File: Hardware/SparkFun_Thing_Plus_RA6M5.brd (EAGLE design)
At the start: 22.9 x 71.1 mm, 93 parts, among them J1 USB Female Type C Connector, J2 THING_PLUS_LOGICAL, J3 QWIIC_RA, J4 CONN_03X2, J7 MICRO-SDFRICTION, Q2 20V/4.2A/52mΩ/1.4W, U1 R7FA6M5, U2 DA14531MOD, U3 MCP73831, U4 RT9080-33GJ5, U5 W25QXX128MBIT-6X5, U6 MCP1501-3.3V, U7 MAX17048, U8 LM66200, Y1 24.000MHz, Y2 32.768kHz

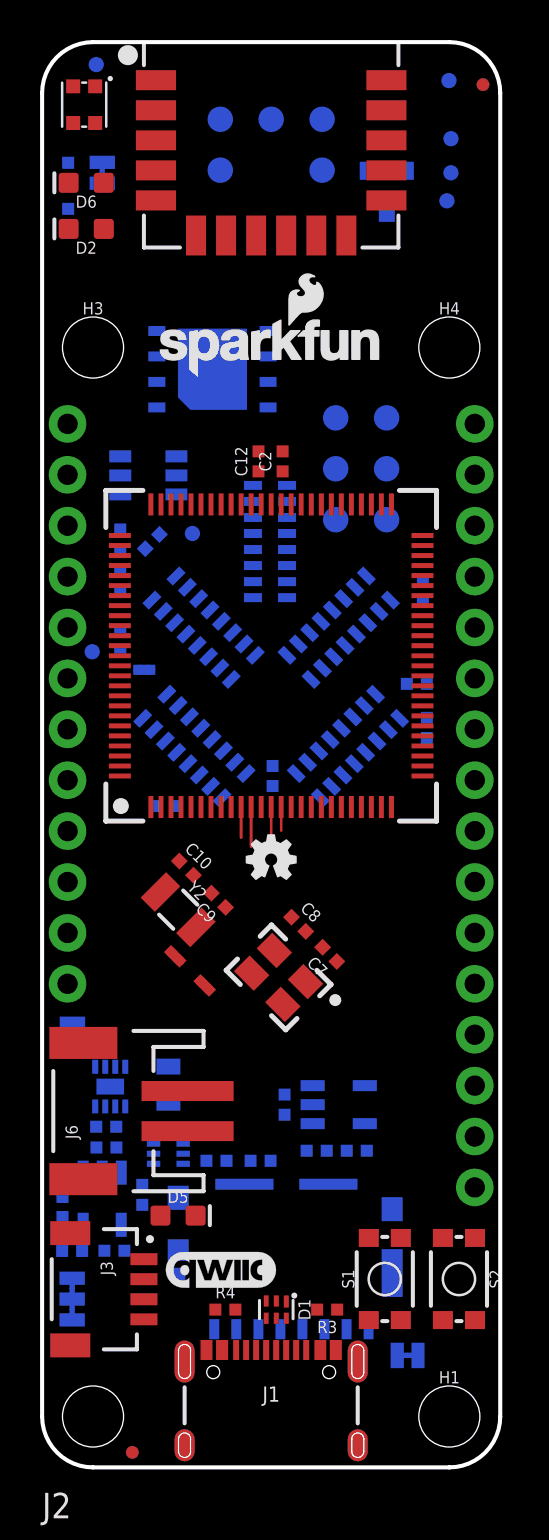
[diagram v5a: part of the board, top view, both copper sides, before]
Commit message: update based on pre-design review comments.
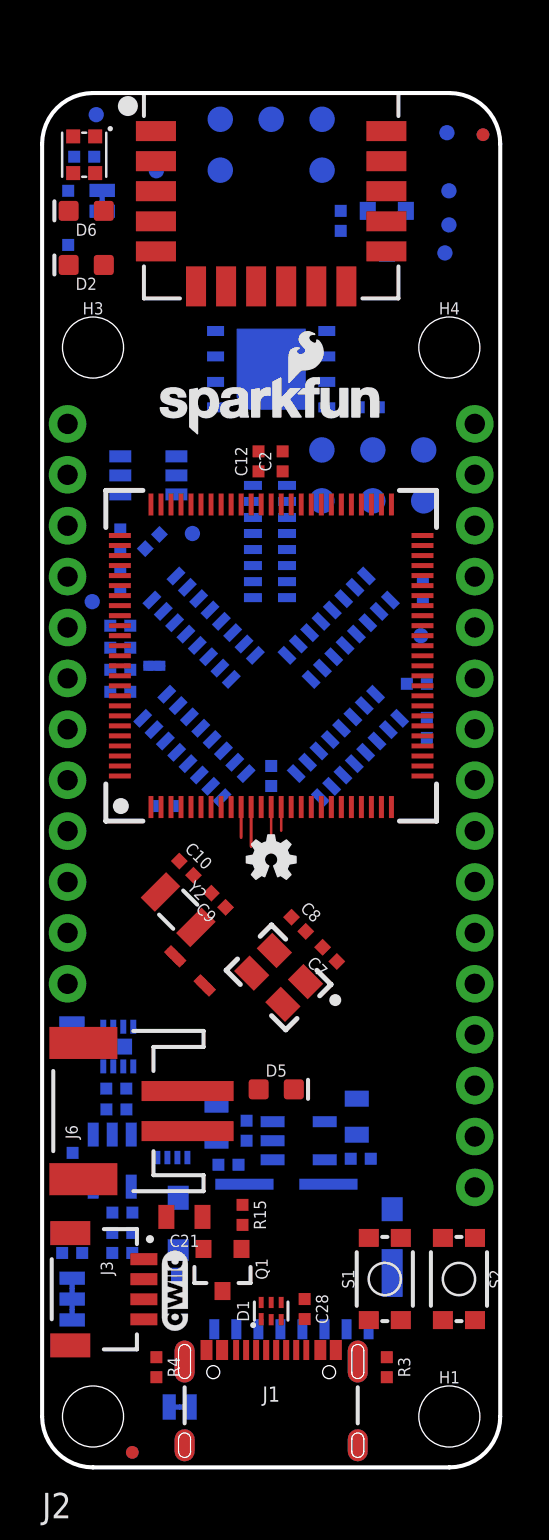
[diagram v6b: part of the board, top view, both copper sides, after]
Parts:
- removed JP1, JP3: JUMPER-SMT_2_NC_TRACE_SILK, SparkFun-Jumpers:SMT-JUMPER_2_NC_TRACE_SILK
- added C21: 10uF, SparkFun-Capacitors:0805
- added C22, C23, C25, C26, C28: 0.1uF, SparkFun-Capacitors:0402-TIGHT
- added C24: 47uF/6.3V, SparkFun-Capacitors:0805
- added C27: 1.0uF, SparkFun-Capacitors:0402-TIGHT
- added CHG, SHLD: JUMPER-SMT_2_NC_TRACE_SILK, SparkFun-Jumpers:SMT-JUMPER_2_NC_TRACE_SILK
- added Q1: 20V/4.2A/52mΩ/1.4W, SparkFun-DiscreteSemi:SOT23-3
- added R13, R15: 1k, SparkFun-Resistors:0402-TIGHT
- added TP9: TEST-POINT3, SparkFun-Connectors:PAD.03X.03
- added U$8: (no value), SparkFun-Aesthetics:SFE_LOGO_FLAME_STOP_.1
- LOGO3: value QWIIC_LOGO_CONNECTOR -> QWIIC_LOGO_4MM; device SparkFun-Aesthetics:QWIIC_5.5MM -> SparkFun-Aesthetics:QWIIC_4MM
- R10: value 10k -> 100k
- moved C1 10.1 mm to (1.50, 11.7), turned to 180 degrees
- moved D5 7.98 mm to (11.7, 18.9)
- moved R1 6.58 mm to (4.00, 10.7), turned to 180 degrees
- moved R4 4.49 mm to (5.70, 5.00), turned to 270 degrees
- moved C14 4.46 mm to (9.30, 15.1), turned to 0 degrees
- moved R3 4.14 mm to (17.2, 5.00), turned to 270 degrees
- moved C20 3.06 mm to (8.70, 17.2)
- moved U5 2.93 mm to (11.4, 54.8)
- moved LOGO2 2.88 mm to (11.4, 53.0)
- moved U4 2.69 mm to (12.8, 16.3)
- moved TP8 2.60 mm to (20.2, 66.6)
- moved TP3 2.60 mm to (20.1, 60.6)
- moved TP5 2.60 mm to (20.3, 63.7)
- moved TP7 2.60 mm to (20.3, 62.0)
- moved U2 2.54 mm to (11.4, 65.7)
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- renumbered JP2 to I2C
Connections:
- removed net N$25: RN3.15, U1.17
- removed net N$29: RN4.16, U1.40
- removed net N$34: RN4.9, U1.58
- removed net N$8: J5.6, Q2.1
- new net !DA14531_RST!: J5.6, R13.1, RN4.9, U1.58
- new net !NMI!: RN4.16, TP9.1, U1.40
- new net !SD_EN!: R15.1, RN3.1, U1.16
- new net 3.3V_SW: C28.2, J7.4, Q1.3
- new net N$4: Q2.1, R13.2
- new net N$47: Q1.1, R15.2
- net 3.3V: now also C21.1, C22.2, C23.2, C24.1, Q1.2, RN3.14, RN3.16, RN4.8; no longer J7.4, RN3.3
- net AGND: now also C25.2, C26.2, C27.2
- net AVCC0: now also C25.1
- net GND: now also C21.2, C22.1, C23.1, C24.2, C28.1, RN3.15, SHLD.1; no longer JP1.1, RN3.1, RN3.2, RN4.8
- net N$1: now also CHG.2; no longer JP3.2
- net N$12: now also RN3.3; no longer RN3.14
- net N$13: now also RN3.2, U1.17; no longer RN3.16, U1.16
- net N$17: now also D1.3; no longer D1.4
- net N$19: now also SHLD.2; no longer JP1.2
- net N$2: now also CHG.1; no longer JP3.1
- net N$7: now also D1.1; no longer D1.6
- net USBD_N: now also D1.4; no longer D1.3
- net USBD_P: now also D1.6; no longer D1.1
- net VREF1: now also C26.1, C27.1
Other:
- board size 22.9 x 71.1 mm -> 22.9 x 68.6 mm

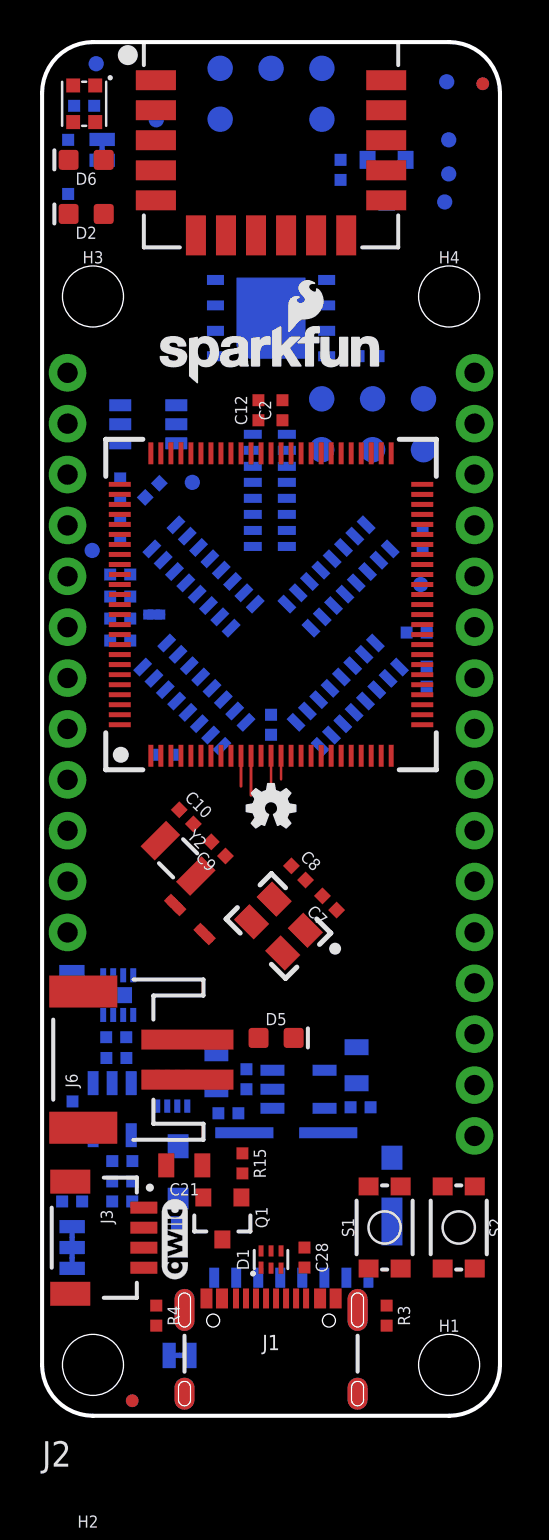
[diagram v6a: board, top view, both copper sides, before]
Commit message: Update Sch, Lbr, & Brd files.
Add broken out resistors for boot/reset pins.
Move array resistors around to make them route easier.
Add BAT jumper.
Add 1u to AVCC net.
Move spare array resistor to bottom.
Pull status pin to 3.3V for LM66200.
Make RT9080 PUR 1M.
Replace VREF with another RT9080.
Rename some nets.
Remove SD card PURs since they're available internally on the processor.
Increased the size of some TPs where there was room.
Routed whole board.
Changed thickness of some silk on parts.
Added PROD_IDs to new parts.
Renamed misnamed device.
Delete unused VREF device.
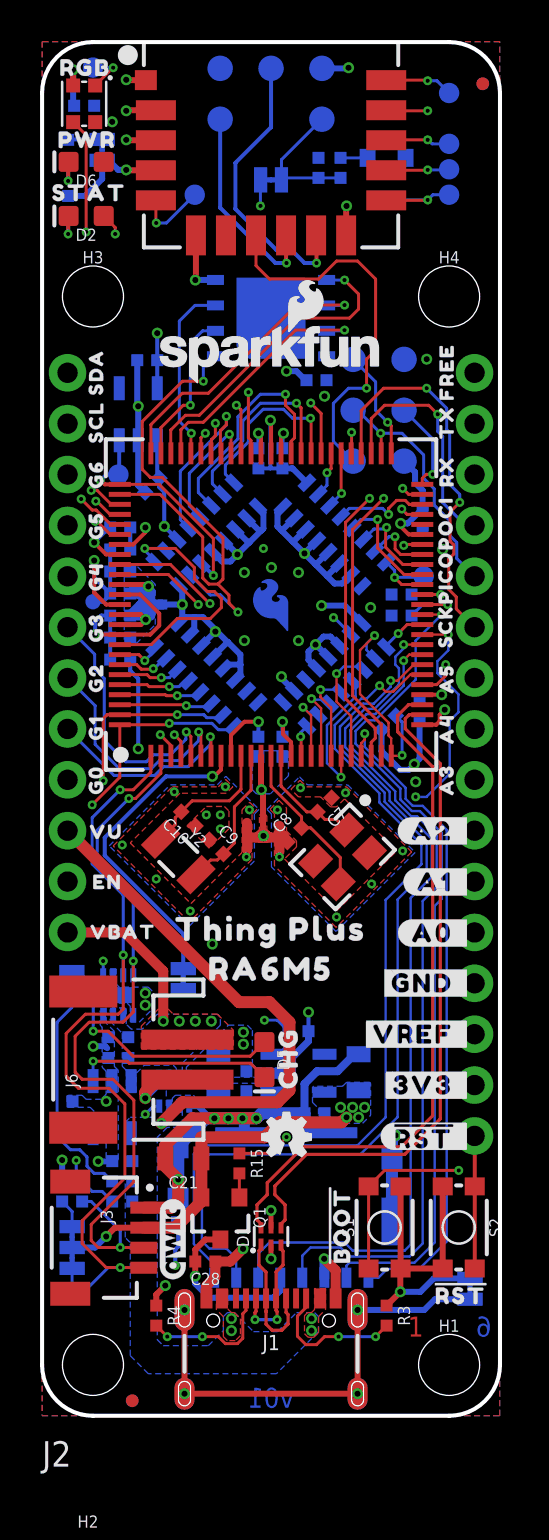
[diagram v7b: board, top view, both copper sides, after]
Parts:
- removed RN2: 10K, SparkFun_Thing_Plus_RA6M5:2506_AR
- added BAT, RST: JUMPER-SMT_2_NC_TRACE_SILK, SparkFun-Jumpers:SMT-JUMPER_2_NC_TRACE_SILK
- added C29: 1.0uF, SparkFun-Capacitors:0402-TIGHT
- added FB2: 120-OHM, SparkFun-Coils:0402-TIGHT
- added R14, R16, R8: 10k, SparkFun-Resistors:0402-TIGHT
- added U$10: (no value), output:SWD_BLE0
- added U$12: (no value), output:#BOOT#0
- added U$13, U$51: (no value), output:#RST#0
- added U$14: (no value), output:CHG0
- added U$15: (no value), output:STAT0
- added U$16: (no value), output:PWR0
- added U$17: (no value), output:RGB0
- added U$18: (no value), output:THING_PLUS0
- added U$19: (no value), output:##RST#_#0
- added U$20: (no value), output:#3V3_#0
- added U$21: (no value), output:#VREF_#0
- added U$22: (no value), output:#GND_#0
- added U$23: (no value), output:#A0_#0
- added U$24: (no value), output:#A1_#0
- added U$25: (no value), output:#A2_#0
- added U$26: (no value), output:A30
- added U$27, U$59: (no value), output:A40
- added U$28, U$60: (no value), output:A50
- added U$29, U$61: (no value), output:SCK0
- added U$30, U$62: (no value), output:PICO0
- added U$31, U$63: (no value), output:POCI0
- added U$32, U$64: (no value), output:RX0
- added U$33, U$65: (no value), output:TX0
- added U$34, U$66: (no value), output:FREE0
- added U$35, U$67: (no value), output:SDA0
- added U$36, U$68: (no value), output:SCL0
- added U$37, U$69: (no value), output:G60
- added U$38, U$70: (no value), output:G50
- added U$39, U$71: (no value), output:G40
- added U$40, U$72: (no value), output:G30
- added U$41, U$73: (no value), output:G20
- added U$42: (no value), output:G10
- added U$43: (no value), output:G00
- added U$44: (no value), output:VU0
- added U$45: (no value), output:EN0
- added U$46: (no value), output:VBAT0
- added U$47: (no value), output:#PWR#0
- added U$48: (no value), output:##RST##0
- added U$49: (no value), output:#BAT#0
- added U$50: (no value), output:#SHLD#0
- added U$52: (no value), output:#_3V3#0
- added U$53: (no value), output:VREF0
- added U$54: (no value), output:#_GND#0
- added U$55: (no value), output:#_A0#0
- added U$56: (no value), output:#_A1#0
- added U$57: (no value), output:#_A2#0
- added U$58: (no value), output:#_A3#0
- added U$74: (no value), output:#G1#0
- added U$75: (no value), output:#G0#0
- added U$76: (no value), output:#VUSB#0
- added U$77: (no value), output:#EN_#0
- added U$78: (no value), output:#VBAT_#0
- added U$79: (no value), output:RA6M50
- added U$80: (no value), SparkFun-Aesthetics:ORDERING_INSTRUCTIONS
- added U$9: (no value), output:SWD_RA6M50
- C19: value 1.0nF -> 1.0uF
- R10: value 100k -> 1M
- TP1, TP2, TP3, TP5, TP6, TP7, TP8, TP9: value TEST-POINT3 -> TEST-POINT3X4; device SparkFun-Connectors:PAD.03X.03 -> SparkFun-Connectors:PAD.03X.04
- U$8: device SparkFun-Aesthetics:SFE_LOGO_FLAME_STOP_.1 -> SparkFun-Aesthetics:SFE_LOGO_FLAME_COPPER_EXPOSED_.1
- U2: device SparkFun_Thing_Plus_RA6M5:DS14531MOD -> SparkFun_Thing_Plus_RA6M5:DA14531MOD
- U6: value MCP1501-3.3V -> RT9080-33GJ5; device SparkFun_Thing_Plus_RA6M5:SOT-23-6 -> SparkFun-IC-Power:SOT23-5
- moved FRAME1 34.1 mm to (53.8, 2.06)
- moved FRAME2 28.4 mm to (24.3, 1.89)
- moved LOGO4 28.4 mm to (23.3, 0.88)
- moved LOGO1 16.4 mm to (12.2, 13.9)
- moved SHLD 14.9 mm to (21.4, 6.34), turned to 270 degrees
- moved C19 6.54 mm to (5.25, 52.7), turned to 0 degrees
- moved SUPPLYTIE3 5.89 mm to (11.5, 28.9), turned to 90 degrees
- moved SUPPLYTIE2 5.17 mm to (10.6, 28.9), turned to 90 degrees
- moved C28 4.95 mm to (8.15, 7.70), turned to 180 degrees
- moved C7 4.91 mm to (14.1, 30.5), turned to 225 degrees
- moved R2 4.71 mm to (17.3, 34.6), turned to 135 degrees
- moved Y1 4.71 mm to (15.0, 27.9), turned to 225 degrees
- moved C11 4.62 mm to (10.8, 33.4), turned to 270 degrees
- moved TP6 4.20 mm to (7.62, 61.0)
- moved RN4 3.91 mm to (14.6, 44.0), turned to 45 degrees
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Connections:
- net N$105 renamed XCIN
- net N$108 renamed XTAL
- net N$110 renamed XCOUT
- net N$115 renamed EXTAL
- net N$17 renamed USBIN_N
- net N$7 renamed USBIN_P
- removed net !BAT_SW!: RN5.16, U1.99, U8.8
- removed net !RESET!: J2.28, J4.6, RN2.10, S2.3, S2.4, U1.38, U2.8
- removed net N$38: RN1.6, U1.92
- removed net N$39: RN4.15, U1.41
- new net !RA6M5_RESET!: J2.28, J4.6, R14.1, S2.3, S2.4, U1.38, U2.8
- new net BAT_SW: RN5.2, U1.99, U8.8
- new net N$23: RN4.15, U1.43
- new net N$25: RST.2, U1.58
- new net N$29: C26.1, C27.1, FB2.1, U1.87, U1.91
- new net N$7: RN1.9, U1.92
- new net N$8: RN3.9, U1.36
- net !DA14531_RST!: now also R16.2, RST.1; no longer RN4.9, U1.58
- net !FG_ALRT!: now also RN5.1; no longer RN5.2
- net !QCS!: now also RN1.7; no longer RN1.10
- net !SD_EN!: now also RN3.16; no longer RN3.1
- net 3.3V: now also BAT.1, R14.2, R16.1, R8.2, RN1.10, RN3.1, RN3.3, RN5.16; no longer RN1.7, RN2.1, RN2.2, RN2.3, RN2.4, RN2.6, RN2.7, RN2.8, RN3.14, RN3.16, RN3.7, RN4.8, U1.8
- net AGND: now also C29.2
- net AVCC0: now also C29.1
- net BOOT/MD: now also R8.1; no longer RN2.9
- net GND: now also RN1.8, RN3.2, RN3.8, RN4.8, RN4.9; no longer RN1.11, RN2.5, RN3.15, U6.3, U6.5
- net N$12: now also RN3.15, U1.17; no longer RN3.3, U1.18
- net N$13: now also RN3.14, U1.18; no longer RN3.2, U1.17
- net N$15: now also RN3.10; no longer RN3.9
- net N$30: now also U1.41; no longer U1.43
- net N$33: now also BAT.2, U1.8; no longer RN2.12, U1.36
- net N$9: now also RN3.7; no longer RN3.8
- net SDCMD: no longer RN2.14
- net SDDAT0: no longer RN2.11
- net SDDAT1: no longer RN3.10
- net SDDAT2: no longer RN2.16
- net SDDAT3: no longer RN2.15
- net SDDET: no longer RN2.13
- net VIN: now also RN1.11, U6.1; no longer RN1.8, RN5.1, U6.6
- net VREF1: now also FB2.2, U6.5; no longer C26.1, C27.1, U1.87, U1.91, U6.1
- net VREFEN: now also RN1.6, U6.3; no longer RN1.9, U6.4
- net V_BATT: now also U8.3; no longer U8.6
- net V_USB: now also U8.6; no longer U8.3
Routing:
- net GND: track 0.00 -> 155.8 mm, vias 0 -> 44
- net BOOT/MD: track 0.00 -> 73.7 mm, vias 0 -> 3
- net !RA6M5_RESET!: track 0.00 -> 71.3 mm, vias 0 -> 2
- net VREF1: track 0.00 -> 61.7 mm, vias 0 -> 3
- net SDA: track 0.00 -> 61.0 mm, vias 0 -> 3
- net SCL: track 0.00 -> 58.1 mm, vias 0 -> 3
- net VIN: track 0.00 -> 49.3 mm, vias 0 -> 3
- net N$9: track 0.00 -> 49.0 mm, vias 0 -> 2
- net SDDAT3: track 0.00 -> 45.2 mm, vias 0 -> 1
- net SDDAT2: track 0.00 -> 44.7 mm, vias 0 -> 1
- net SDCMD: track 0.00 -> 44.2 mm, vias 0 -> 1
- net SDDET: track 0.00 -> 42.6 mm, vias 0 -> 3
- net SDDAT0: track 0.00 -> 42.0 mm, vias 0 -> 1
- net SDCLK: track 0.00 -> 41.5 mm, vias 0 -> 1
- net USBD_P: track 0.00 -> 34.3 mm
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- added copper zone on layer 1, net 3.3V
- added copper zone on layer 16, net 3.3V
- added copper zone on layer 16, net AGND
- added copper zone on layer 1, net GND
- added copper zone on layer 15, net GND
- added copper zone on layer 16, net GND
- added copper zone on layer 2, net GND
- added copper zone on layer 14, net GND_1
- added copper zone on layer 15, net GND_2
- added copper zone on layer 1, net GND_24
- added copper zone on layer 16, net GND_24
- added copper zone on layer 3, net GND_24
- added copper zone on layer 2, net GND_3
- added copper zone on layer 1, net GND_32
- added copper zone on layer 16, net GND_32
- added copper zone on layer 3, net GND_32
- added copper zone on layer 14, net GND_4
- added copper zone on layer 15, net GND_5
- added copper zone on layer 2, net GND_6
- added copper zone on layer 16, net VIN
- added copper zone on layer 1, net V_BATT
- added copper zone on layer 16, net V_BATT
- added copper zone on layer 1, net V_USB
- added copper zone on layer 16, net V_USB
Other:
- board text added: "1"
- board text added: "2"
- board text added: "3"
- board text added: "4"
- board text added: "5"
- board text added: "6"
- board text added: "Alex Brudner"
- board text added: "All Units in Inches"
- board text added: "Layers: 6 Stackup: JLC06161H-3313 Material: TG155 Outer Layers: 1oz Innter Layers: 0.5oz Board thickness: 1.6mm Via Covering: Epoxy Filled & Capped Soldermask: Red Silkscreen: White Surface Finish: ENIG"
- board text added: "v01"
